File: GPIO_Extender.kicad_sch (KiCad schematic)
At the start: 21 parts, among them IC1 PCA9575PW2,118

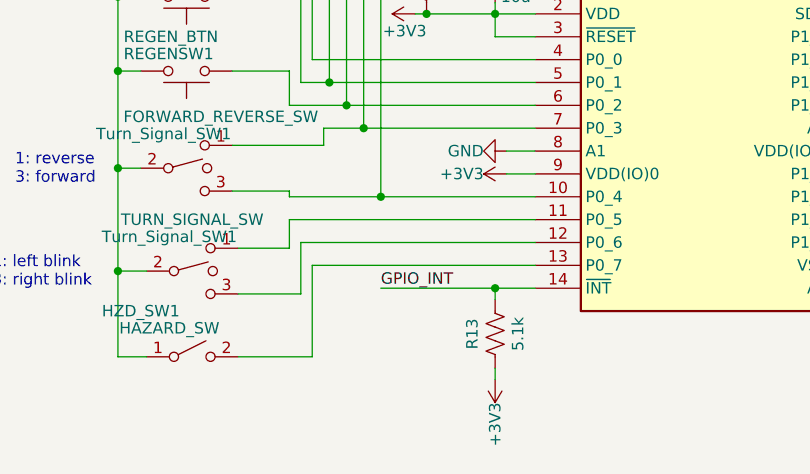
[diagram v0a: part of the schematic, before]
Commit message: assigned footprints
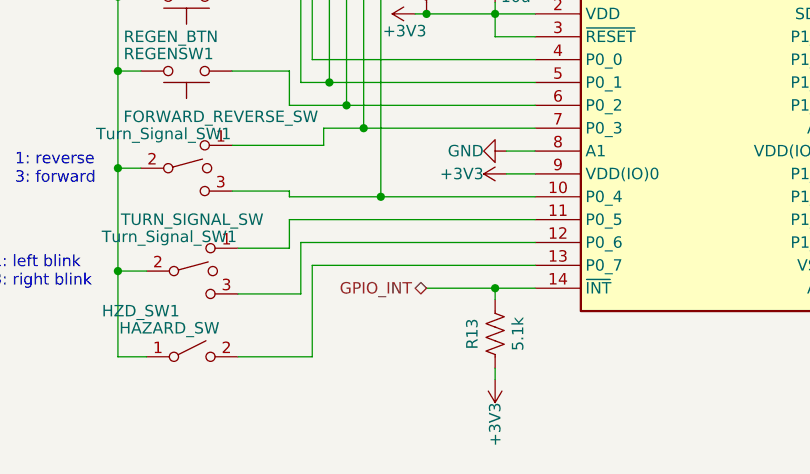
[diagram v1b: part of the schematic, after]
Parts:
- C10, C4, C5, C6, C7, C8, C9: footprint (none) -> Capacitor_SMD:C_0805_2012Metric
- IC1: footprint SOP65P640X110-28N -> UTSVT_ICs:SOT361
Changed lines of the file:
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@@
     (stroke (width 0) (type default))
   )
-  (wire (pts (xy 140.335 129.54) (xy 127.635 129.54))
+  (wire (pts (xy 140.335 129.54) (xy 132.715 129.54))
     (stroke (width 0) (type default))
   )
@@
     (effects (font (size 2.54 2.54) (thickness 0.508) bold) (justify left bottom))
   )
-  (label "GPIO_INT" (at 127.635 129.54 0) (fields_autoplaced)
-    (effects (font (size 1.27 1.27)) (justify left bottom))
+  (hierarchical_label "GPIO_INT" (shape bidirectional) (at 132.715 129.54 180) (fields_autoplaced)
+    (effects (font (size 1.27 1.27)) (justify right))
   )
   (hierarchical_label "LEFT_BLINK" (shape output) (at 200.025 104.14 0) (fields_autoplaced)
@@
       (effects (font (size 1.27 1.27)) (justify left))
     )
-    (property "Footprint" "" (at 123.825 52.705 0)
+    (property "Footprint" "Capacitor_SMD:C_0805_2012Metric" (at 123.825 52.705 0)
       (effects (font (size 1.27 1.27)) hide)
     )
@@
       (effects (font (size 1.27 1.27)))
     )
-    (property "Footprint" "SOP65P640X110-28N" (at 179.07 191.44 0)
+    (property "Footprint" "UTSVT_ICs:SOT361" (at 179.07 191.44 0)
       (effects (font (size 1.27 1.27)) (justify left top) hide)
     )
@@
       (effects (font (size 1.27 1.27)) (justify left))
     )
-    (property "Footprint" "" (at 140.335 95.25 0)
+    (property "Footprint" "Capacitor_SMD:C_0805_2012Metric" (at 140.335 95.25 0)
       (effects (font (size 1.27 1.27)) hide)
     )
@@
       (effects (font (size 1.27 1.27)) (justify left))
     )
-    (property "Footprint" "" (at 142.875 52.705 0)
+    (property "Footprint" "Capacitor_SMD:C_0805_2012Metric" (at 142.875 52.705 0)
       (effects (font (size 1.27 1.27)) hide)
     )
@@
       (effects (font (size 1.27 1.27)) (justify left))
     )
-    (property "Footprint" "" (at 104.14 52.705 0)
+    (property "Footprint" "Capacitor_SMD:C_0805_2012Metric" (at 104.14 52.705 0)
       (effects (font (size 1.27 1.27)) hide)
     )
@@
       (effects (font (size 1.27 1.27)) (justify left))
     )
-    (property "Footprint" "" (at 113.665 52.705 0)
+    (property "Footprint" "Capacitor_SMD:C_0805_2012Metric" (at 113.665 52.705 0)
       (effects (font (size 1.27 1.27)) hide)
     )
@@
       (effects (font (size 1.27 1.27)) (justify left))
     )
-    (property "Footprint" "" (at 133.35 52.705 0)
+    (property "Footprint" "Capacitor_SMD:C_0805_2012Metric" (at 133.35 52.705 0)
       (effects (font (size 1.27 1.27)) hide)
     )
@@
       (effects (font (size 1.27 1.27)) (justify left))
     )
-    (property "Footprint" "" (at 200.025 118.11 0)
-      (effects (font (size 1.27 1.27)) hide)
-    )
+    (property "Footprint" "Capacitor_SMD:C_0805_2012Metric" (at 200.025 118.11 0)
+      (effects (font (size 1.27 1.27)) hide)
+    )

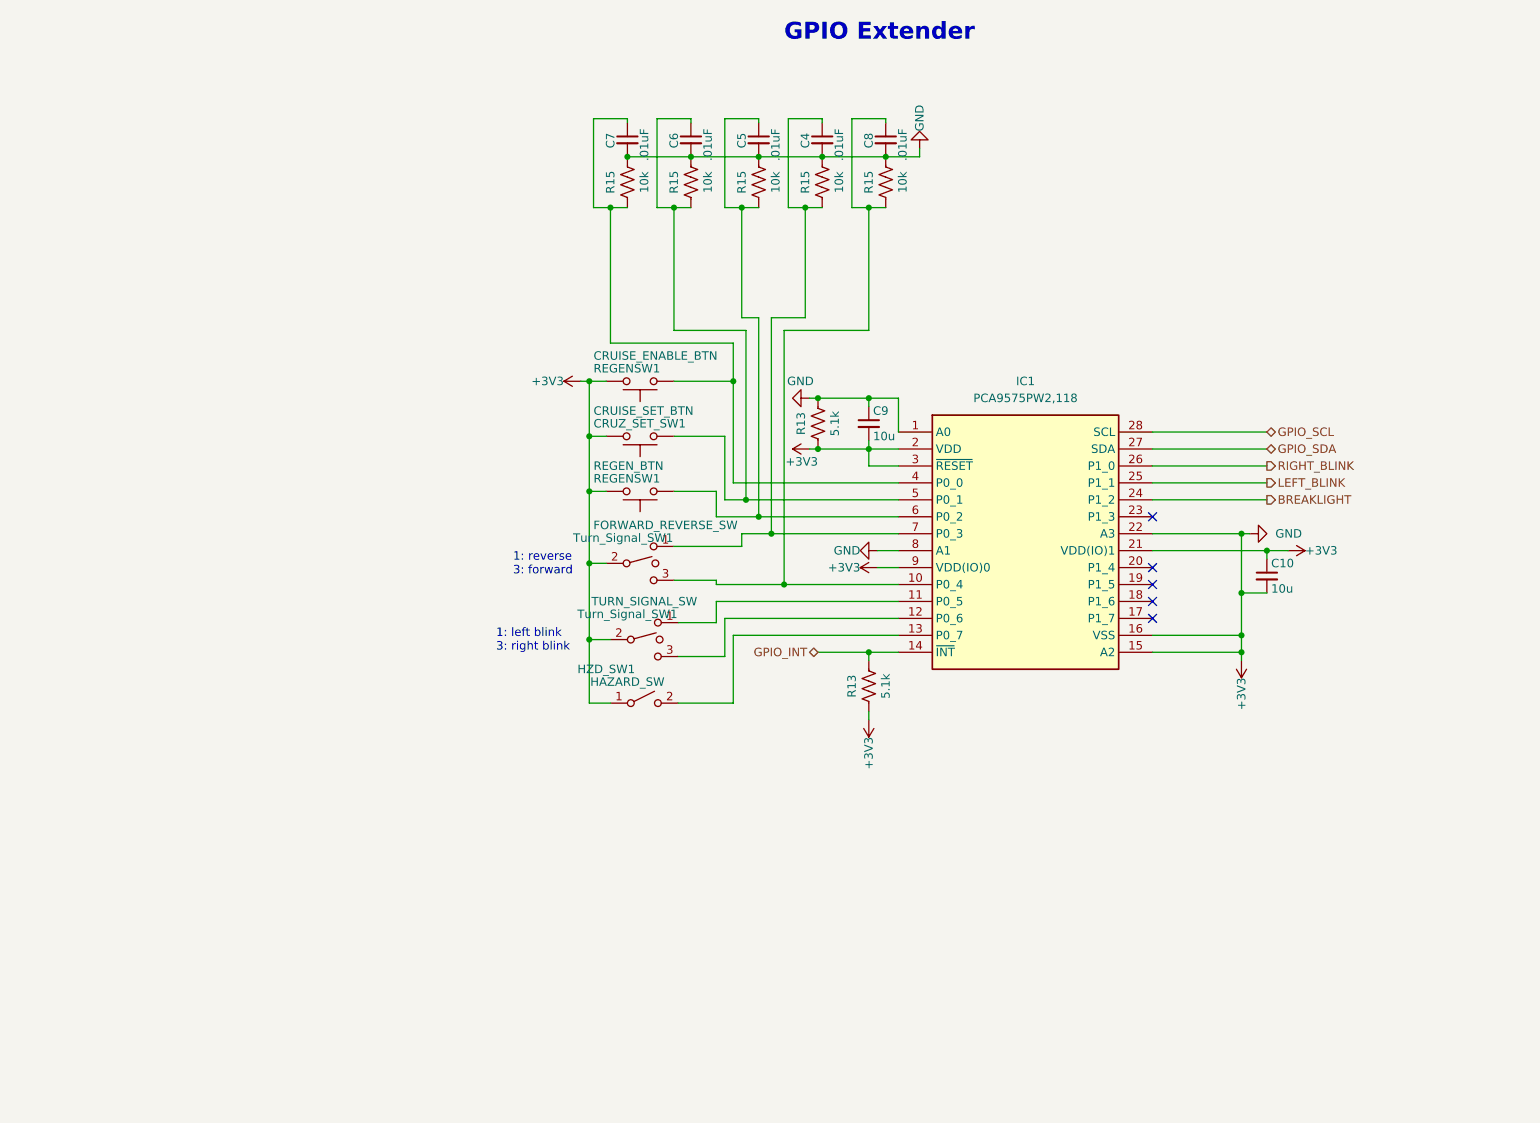
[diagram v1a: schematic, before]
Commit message: organized schematic, changed resistor values, moved ignition signals to IC
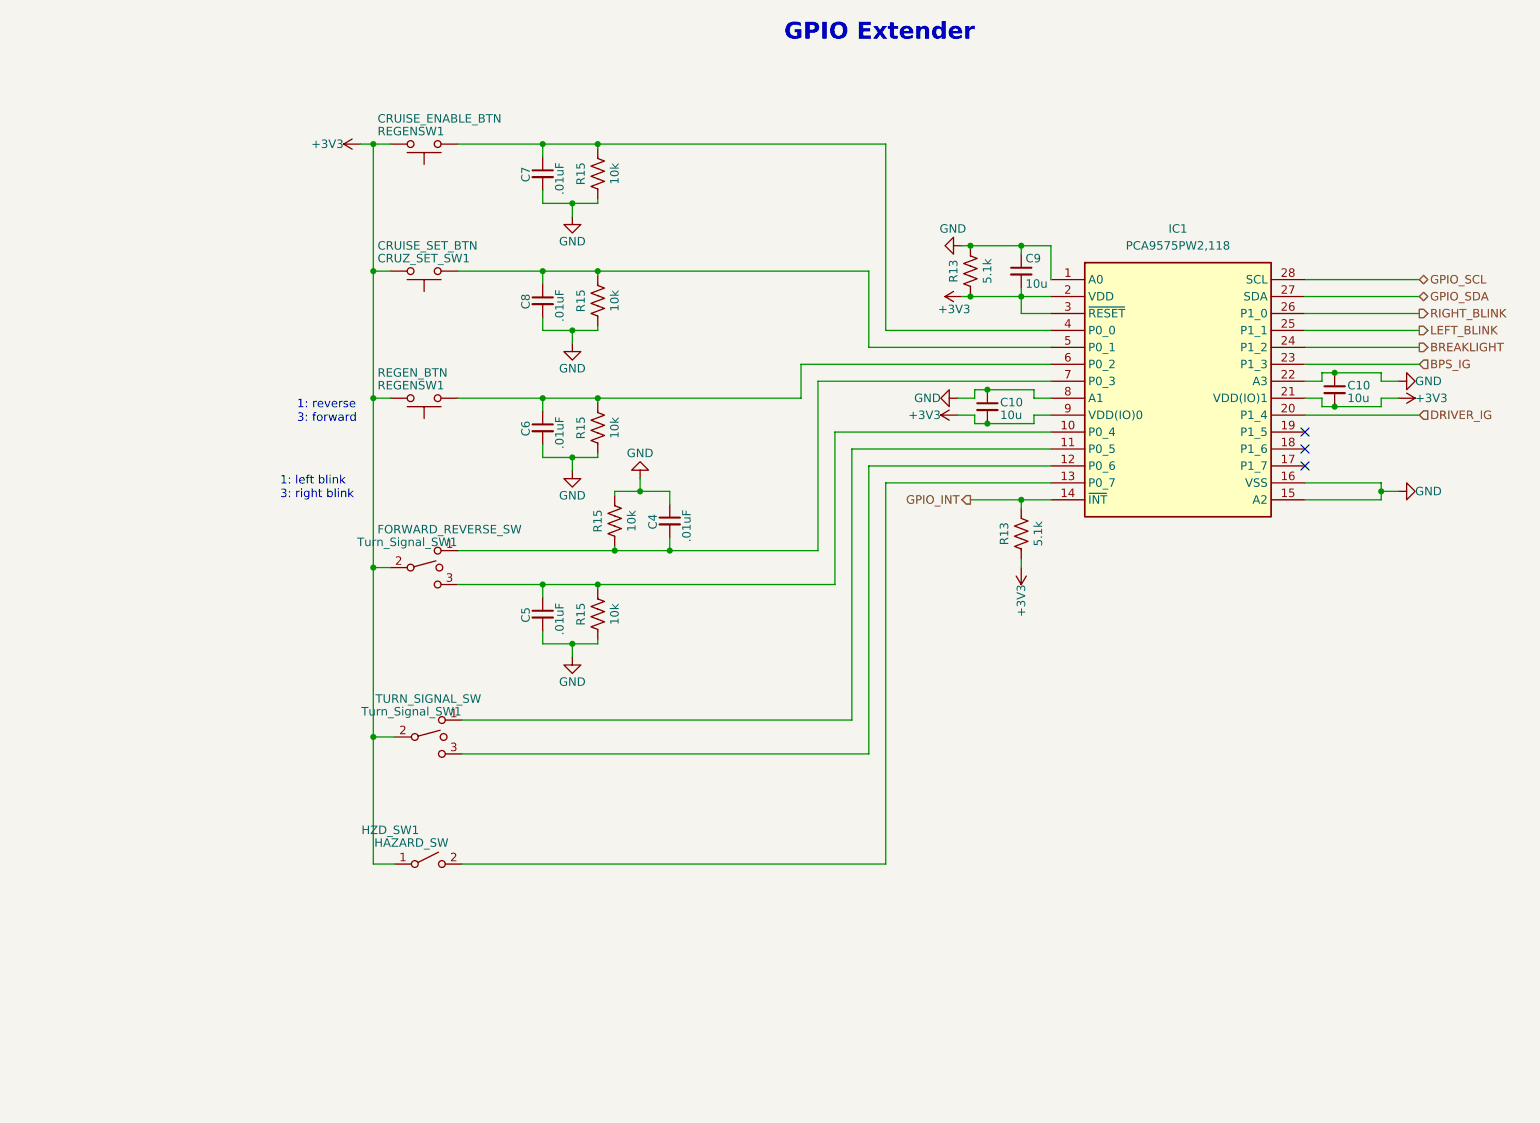
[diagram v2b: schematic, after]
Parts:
- removed C10: 10u, Capacitor_SMD:C_0805_2012Metric, symbol Device:C_Small
- removed R15 (x5): 10k, Resistor_SMD:R_0805_2012Metric, symbol Device:R_US
- added C10 (x2): 10u, Capacitor_SMD:C_0805_2012Metric, symbol Device:C_Small
- added R15 (x5): 10k, Resistor_SMD:R_0805_2012Metric, symbol Device:R_US
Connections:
- net +3V3: now also C10.2, C10.2; no longer C4.2, C5.2, C6.2, C7.2, C8.2, C9.1, IC1.1 (A0), IC1.15 (A2), IC1.16 (VSS), IC1.22 (A3), IC1.8 (A1), R13.1
- net at IC1.6 (P0_2), REGENSW1.1: now also C6.1, R15.1; no longer C5.1
- net at IC1.10 (P0_4), Turn_Signal_SW1.3: now also C5.1, R15.1; no longer C8.1
- net DRIVER_IG: now reaches IC1.20 (P1_4)
- net BPS_IG: now reaches IC1.23 (P1_3)
- net at C7.1, IC1.4 (P0_0), REGENSW1.1: now also R15.1
- net at CRUZ_SET_SW1.1, IC1.5 (P0_1): now also C8.1, R15.1; no longer C6.1
- net at IC1.7 (P0_3), Turn_Signal_SW1.1: now also C4.2, R15.2; no longer C4.1
- new net GND: C10.1, C10.1, C4.1, C5.2, C6.2, C7.2, C8.2, C9.1, IC1.1 (A0), IC1.15 (A2), IC1.16 (VSS), IC1.22 (A3), IC1.8 (A1), R13.1, R15.1, R15.2, R15.2, R15.2, R15.2
- no-connect marks 5 -> 3
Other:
- moved on the sheet: C9, CRUZ_SET_SW1, HZD_SW1, IC1, R13, REGENSW1, Turn_Signal_SW1

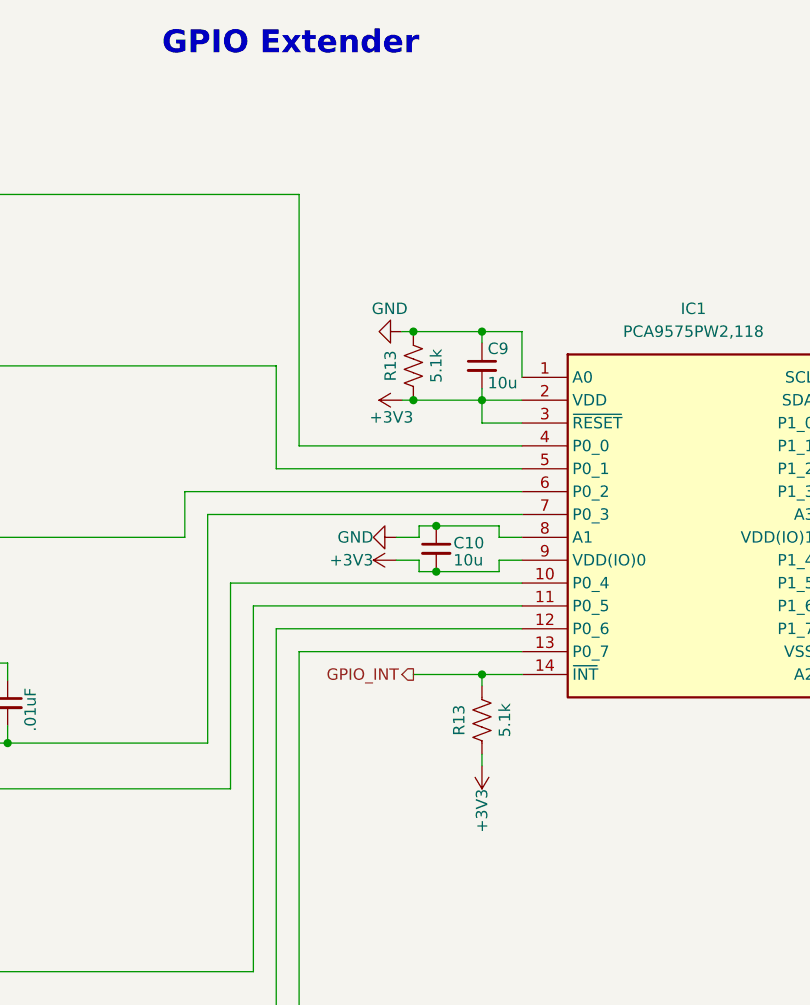
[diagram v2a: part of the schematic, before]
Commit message: Organized schematic, added reset function to extender, changed footprints
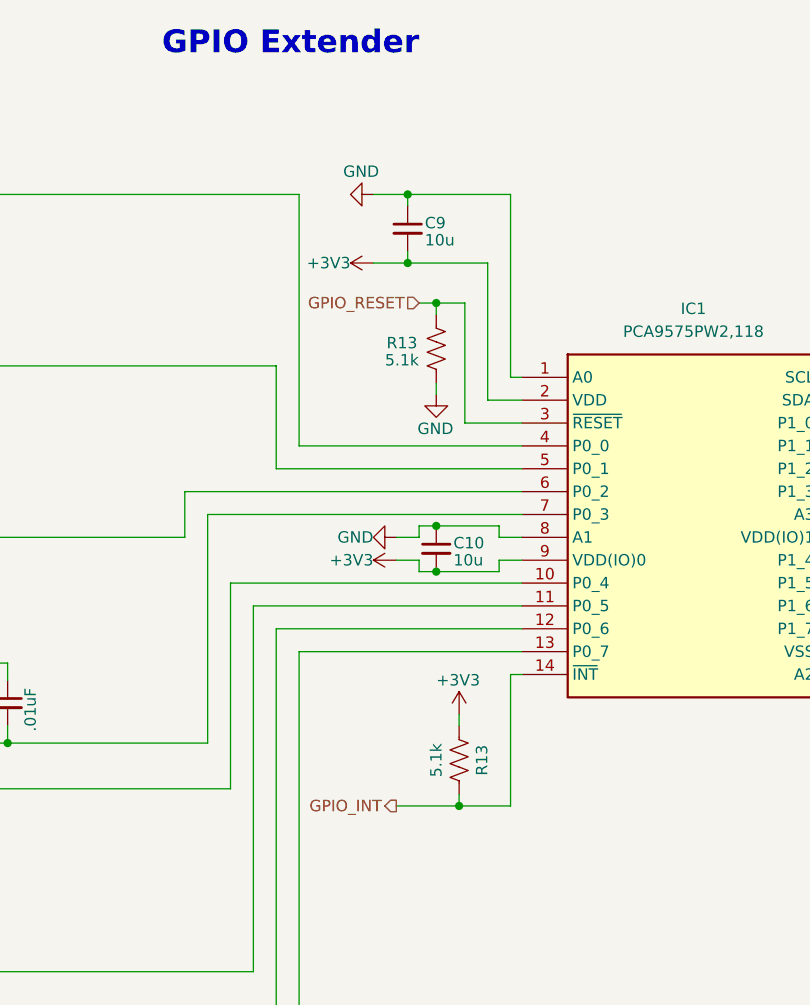
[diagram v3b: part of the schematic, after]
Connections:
- net +3V3: no longer IC1.3 (~{RESET}), R13.2
- net GND: now also R13.2; no longer R13.1
- new net GPIO_RESET: IC1.3 (~{RESET}), R13.1
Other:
- moved on the sheet: C9, R13
